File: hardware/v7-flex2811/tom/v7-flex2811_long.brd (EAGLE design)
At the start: 155 x 7.8 mm, 160 parts

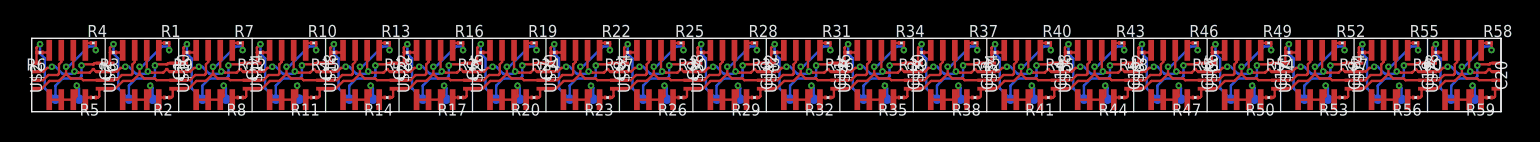
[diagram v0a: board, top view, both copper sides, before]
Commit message: Rebuild a 32 strip from the slightly update single
Single has more room to place passives and slightly smaller
2818 pads so that there's more clearance with the edge
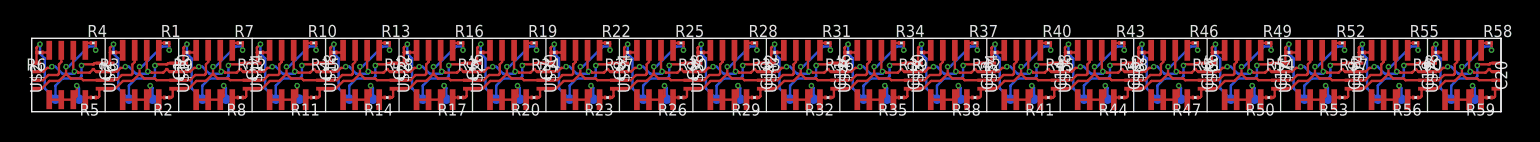
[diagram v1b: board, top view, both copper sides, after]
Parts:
- U$2: device adafruit:SO08 -> Sparky:SO08
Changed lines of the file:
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@@
 <?xml version="1.0" encoding="utf-8"?>
 <!DOCTYPE eagle SYSTEM "eagle.dtd">
-<eagle version="6.5.0">
+<eagle version="7.3.0">
 <drawing>
 <settings>
@@
 <layer number="49" name="Reference" color="7" fill="1" visible="no" active="yes"/>
 <layer number="50" name="dxf" color="7" fill="1" visible="no" active="no"/>
-<layer number="51" name="tDocu" color="7" fill="1" visible="no" active="yes"/>
+<layer number="51" name="tDocu" color="7" fill="1" visible="yes" active="yes"/>
 <layer number="52" name="bDocu" color="7" fill="1" visible="no" active="yes"/>
 <layer number="53" name="tGND_GNDA" color="7" fill="9" visible="no" active="no"/>
@@
 </class>
 </classes>
-<designrules name="default *">
+<designrules name="PCBWayMin *">
 <description language="de">&lt;b&gt;EAGLE Design Rules&lt;/b&gt;
 &lt;p&gt;
@@
 <param name="mdViaViaSameLayer" value="8mil"/>
 <param name="mnLayersViaInSmd" value="2"/>
-<param name="mdCopperDimension" value="40mil"/>
+<param name="mdCopperDimension" value="10mil"/>
 <param name="mdDrill" value="8mil"/>
 <param name="mdSmdStop" value="0mil"/>
 <param name="msWidth" value="6mil"/>
-<param name="msDrill" value="3mil"/>
+<param name="msDrill" value="0.3mm"/>
 <param name="msMicroVia" value="9.99mm"/>
 <param name="msBlindViaRatio" value="0.5"/>
@@
 <param name="rlMinPadBottom" value="10mil"/>
 <param name="rlMaxPadBottom" value="20mil"/>
-<param name="rlMinViaOuter" value="8mil"/>
+<param name="rlMinViaOuter" value="6mil"/>
 <param name="rlMaxViaOuter" value="20mil"/>
-<param name="rlMinViaInner" value="8mil"/>
+<param name="rlMinViaInner" value="6mil"/>
 <param name="rlMaxViaInner" value="20mil"/>
 <param name="rlMinMicroViaOuter" value="4mil"/>
@@
 <param name="mlMinCreamFrame" value="0mil"/>
 <param name="mlMaxCreamFrame" value="0mil"/>
-<param name="mlViaStopLimit" value="0mil"/>
+<param name="mlViaStopLimit" value="25mil"/>
 <param name="srRoundness" value="0"/>
 <param name="srMinRoundness" value="0mil"/>
@@
 <pass name="Default">
 <param name="RoutingGrid" value="50mil"/>
+<param name="AutoGrid" value="1"/>
+<param name="Efforts" value="0"/>
+<param name="TopRouterVariant" value="1"/>
 <param name="tpViaShape" value="round"/>
 <param name="PrefDir.1" value="|"/>
@@
 <element name="C2" library="rcl" package="C0201" value="" x="6.5" y="4.75" rot="R270"/>
 <element name="U$1" library="tom-tappytap-v5-flex" package="TP_4MM_MED_PAD" value="TP_4MM_MED_PAD" x="3.75" y="3.875" rot="MR0"/>
-<element name="U$2" library="adafruit" package="SO08" value="WS2818" x="3.75" y="3.875"/>
+<element name="U$2" library="Sparky" package="SO08" value="WS2818" x="3.75" y="3.875"/>
 <element name="R4" library="rcl" package="R0201" value="" x="6.5" y="7.25"/>
 <element name="R5" library="rcl" package="R0201" value="" x="6.5" y="1.5" rot="R180"/>
@@
 </signal>
 </signals>
+<errors>
+</errors>
 </board>
 </drawing>
